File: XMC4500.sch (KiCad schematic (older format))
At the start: 1 part

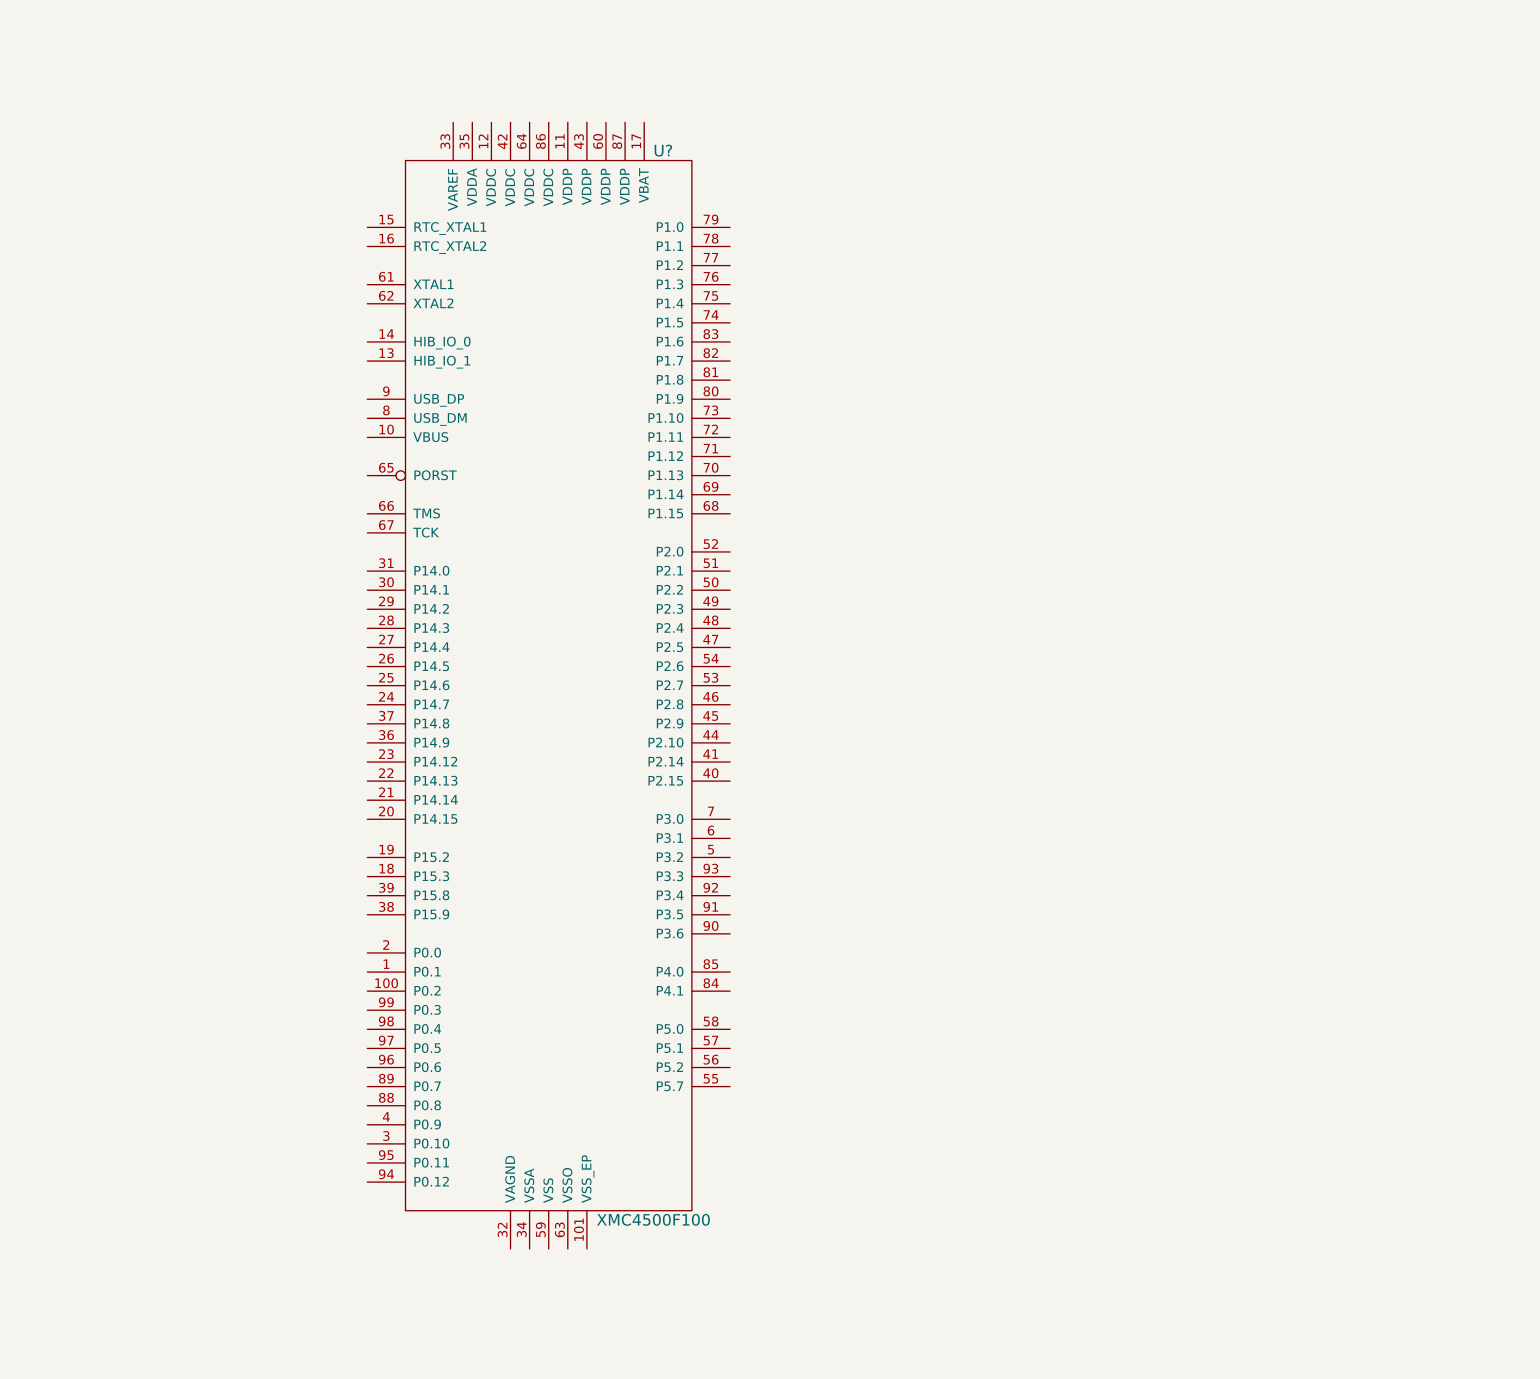
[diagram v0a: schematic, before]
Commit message: Added capacitors for XMC chip, diagram of power tree, and more connectors.
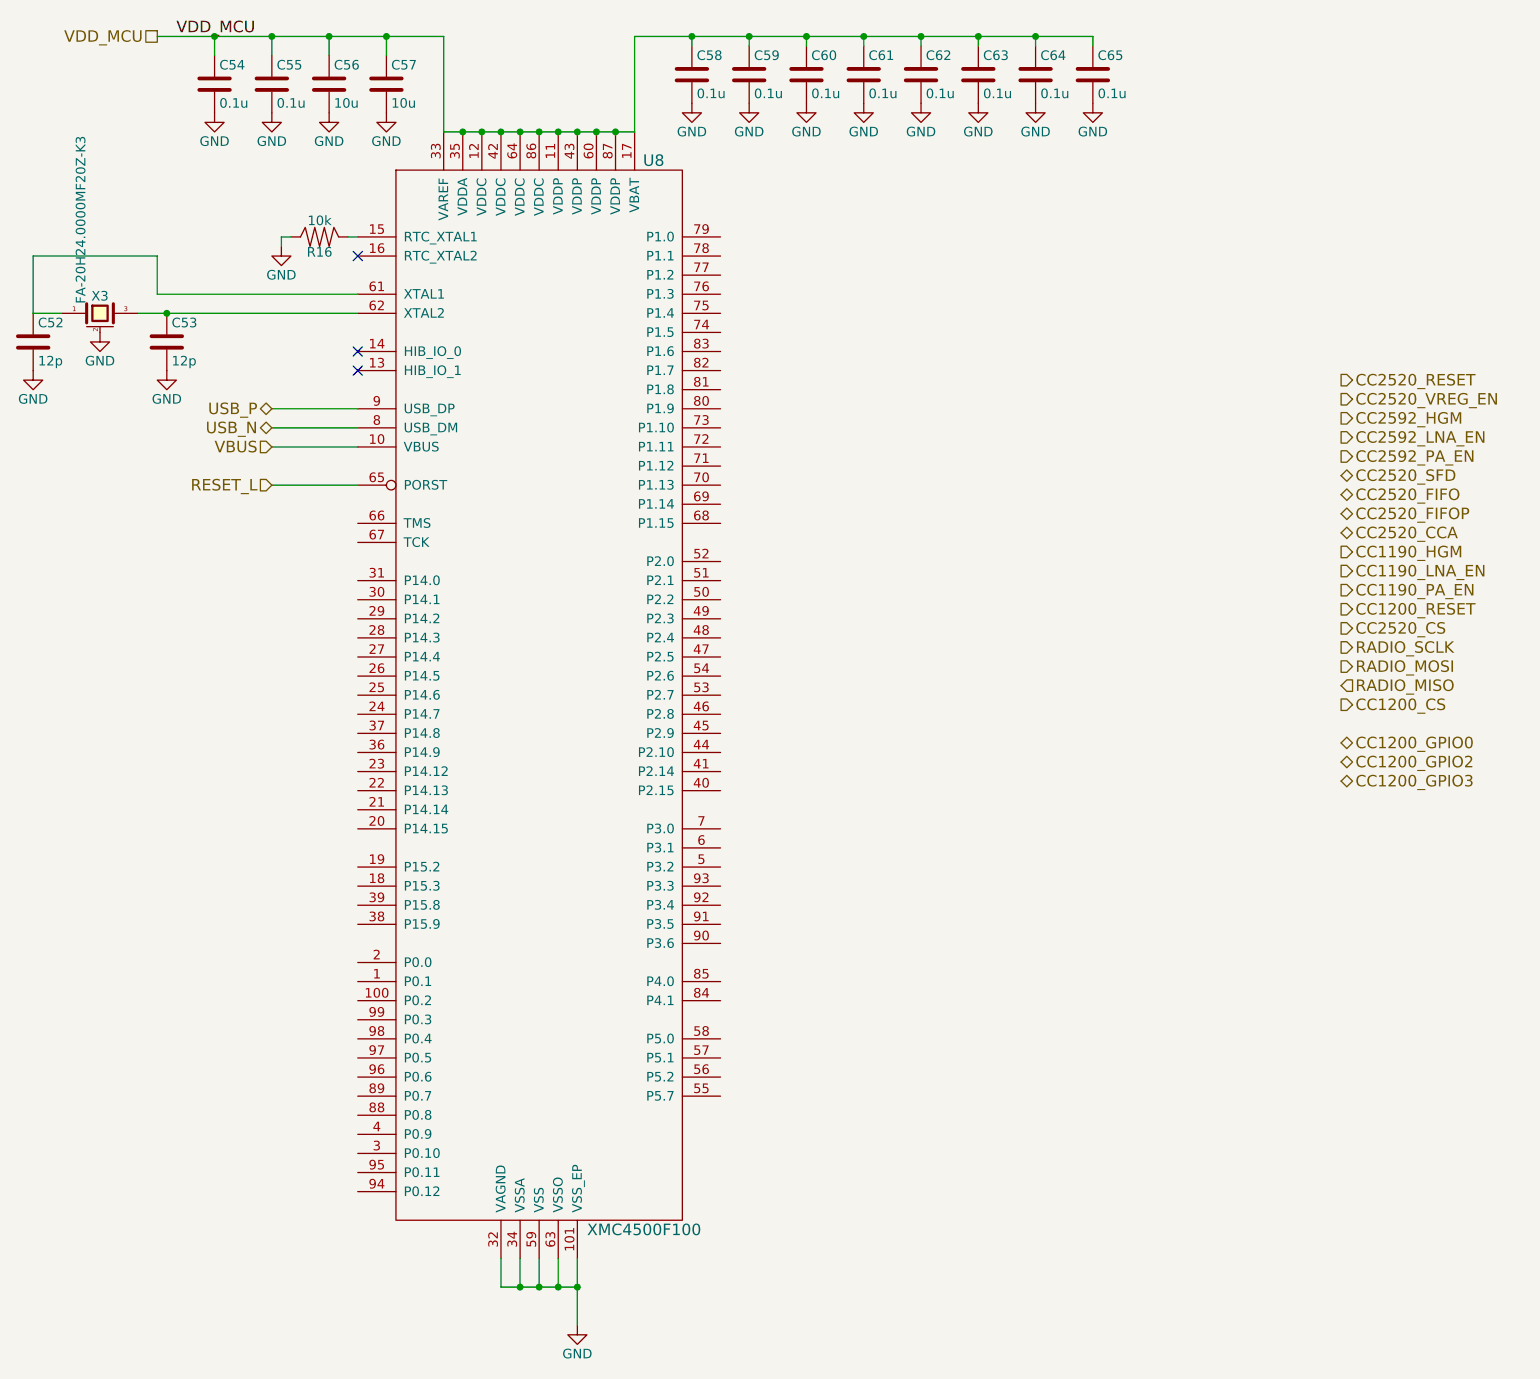
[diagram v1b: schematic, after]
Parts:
- removed U?: XMC4500F100, symbol XMC4500F100
- added C52, C53: 12p, Capacitors_SMD:C_0402, symbol C
- added C54, C55, C58, C59, C60, C61, C62, C63, C64, C65: 0.1u, Capacitors_SMD:C_0402, symbol C
- added C56, C57: 10u, Capacitors_SMD:C_0603, symbol C
- added R16: 10k, Resistors_SMD:R_0402, symbol R
- added U8: XMC4500F100, Housings_QFP:LQFP-100-1EP_14x14mm_Pitch0.5mm, symbol XMC4500F100
- added X3: FA-20H24.0000MF20Z-K3, Crystals_Oscillators_SMD:FA-20H, symbol CRYSTAL_SMD
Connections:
- new net: R16.1, U8.15 (RTC_XTAL1)
- new net: C52.1, U8.61 (XTAL1), X3.1
- new net: C53.1, U8.62 (XTAL2), X3.3
- new net GND: C52.2, C53.2, C54.2, C55.2, C56.2, C57.2, C58.2, C59.2, C60.2, C61.2, C62.2, C63.2, C64.2, C65.2, R16.2, U8.101 (VSS_EP), U8.32 (VAGND), U8.34 (VSSA), U8.59 (VSS), U8.63 (VSSO), X3.2 (gnd), X3.4 (gnd)
- new net RESET_L: U8.65 (PORST)
- new net USB_N: U8.8 (USB_DM)
- new net USB_P: U8.9 (USB_DP)
- new net VBUS: U8.10 (VBUS)
- new net VDD_MCU: C54.1, C55.1, C56.1, C57.1, C58.1, C59.1, C60.1, C61.1, C62.1, C63.1, C64.1, C65.1, U8.11 (VDDP), U8.12 (VDDC), U8.17 (VBAT), U8.33 (VAREF), U8.35 (VDDA), U8.42 (VDDC), U8.43 (VDDP), U8.60 (VDDP), U8.64 (VDDC), U8.86 (VDDC), U8.87 (VDDP)
- no-connect marks 0 -> 3

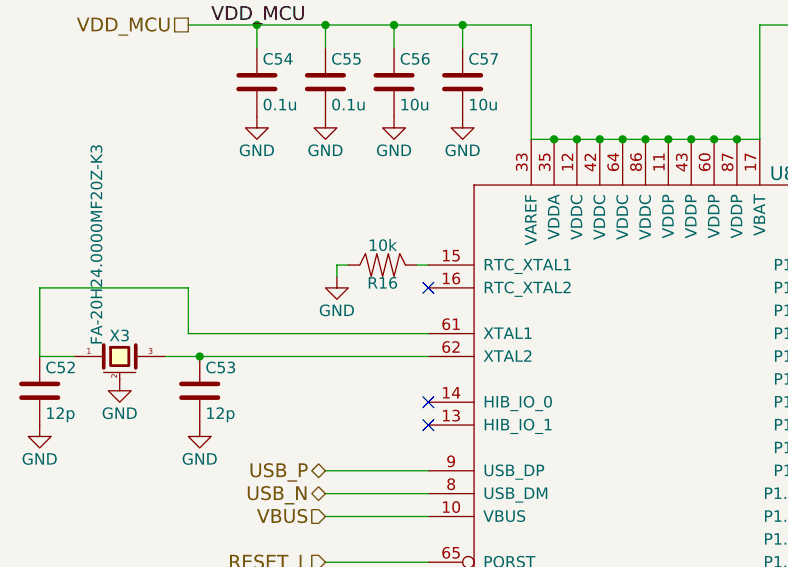
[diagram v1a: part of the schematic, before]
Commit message: Added 3.3V LDO
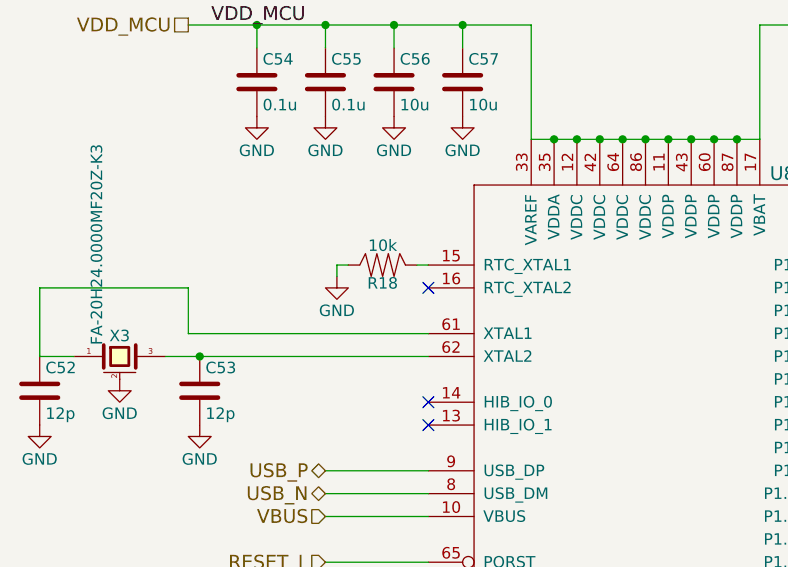
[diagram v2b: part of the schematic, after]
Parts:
- renumbered R16 to R18
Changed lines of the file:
@@
 $Descr A4 11693 8268
 encoding utf-8
-Sheet 4 4
+Sheet 4 7
 Title ""
 Date ""
@@
 $EndComp
 $Comp
-L GND #PWR80
+L GND #PWR080
 U 1 1 55BD550B
 P 4500 7450
-F 0 "#PWR80" H 4500 7200 50  0001 C CNN
+F 0 "#PWR080" H 4500 7200 50  0001 C CNN
 F 1 "GND" H 4500 7300 50  0000 C CNN
 F 2 "" H 4500 7450 60  0000 C CNN
@@
 $EndComp
 $Comp
-L GND #PWR81
+L GND #PWR081
 U 1 1 55BD5744
 P 5100 1050
-F 0 "#PWR81" H 5100 800 50  0001 C CNN
+F 0 "#PWR081" H 5100 800 50  0001 C CNN
 F 1 "GND" H 5100 900 50  0000 C CNN
 F 2 "" H 5100 1050 60  0000 C CNN
@@
 $EndComp
 $Comp
-L GND #PWR82
+L GND #PWR082
 U 1 1 55BD5822
 P 5400 1050
-F 0 "#PWR82" H 5400 800 50  0001 C CNN
+F 0 "#PWR082" H 5400 800 50  0001 C CNN
 F 1 "GND" H 5400 900 50  0000 C CNN
 F 2 "" H 5400 1050 60  0000 C CNN
@@
 $EndComp
 $Comp
-L GND #PWR83
+L GND #PWR083
 U 1 1 55BD589D
 P 5700 1050
-F 0 "#PWR83" H 5700 800 50  0001 C CNN
+F 0 "#PWR083" H 5700 800 50  0001 C CNN
 F 1 "GND" H 5700 900 50  0000 C CNN
 F 2 "" H 5700 1050 60  0000 C CNN
@@
 $EndComp
 $Comp
-L GND #PWR84
+L GND #PWR084
 U 1 1 55BD58A9
 P 6000 1050
-F 0 "#PWR84" H 6000 800 50  0001 C CNN
+F 0 "#PWR084" H 6000 800 50  0001 C CNN
 F 1 "GND" H 6000 900 50  0000 C CNN
 F 2 "" H 6000 1050 60  0000 C CNN
@@
 $EndComp
 $Comp
-L GND #PWR85
+L GND #PWR085
 U 1 1 55BD5AC7
 P 6300 1050
-F 0 "#PWR85" H 6300 800 50  0001 C CNN
+F 0 "#PWR085" H 6300 800 50  0001 C CNN
 F 1 "GND" H 6300 900 50  0000 C CNN
 F 2 "" H 6300 1050 60  0000 C CNN
@@
 $EndComp
 $Comp
-L GND #PWR86
+L GND #PWR086
 U 1 1 55BD5AD3
 P 6600 1050
-F 0 "#PWR86" H 6600 800 50  0001 C CNN
+F 0 "#PWR086" H 6600 800 50  0001 C CNN
 F 1 "GND" H 6600 900 50  0000 C CNN
 F 2 "" H 6600 1050 60  0000 C CNN
@@
 $EndComp
 $Comp
-L GND #PWR87
+L GND #PWR087
 U 1 1 55BD5ADF
 P 6900 1050
-F 0 "#PWR87" H 6900 800 50  0001 C CNN
+F 0 "#PWR087" H 6900 800 50  0001 C CNN
 F 1 "GND" H 6900 900 50  0000 C CNN
 F 2 "" H 6900 1050 60  0000 C CNN
@@
 $EndComp
 $Comp
-L GND #PWR88
+L GND #PWR088
 U 1 1 55BD5AEB
 P 7200 1050
-F 0 "#PWR88" H 7200 800 50  0001 C CNN
+F 0 "#PWR088" H 7200 800 50  0001 C CNN
 F 1 "GND" H 7200 900 50  0000 C CNN
 F 2 "" H 7200 1050 60  0000 C CNN
@@
 $EndComp
 $Comp
-L GND #PWR78
+L GND #PWR089
 U 1 1 55BD5E40
 P 3200 1100
-F 0 "#PWR78" H 3200 850 50  0001 C CNN
+F 0 "#PWR089" H 3200 850 50  0001 C CNN
 F 1 "GND" H 3200 950 50  0000 C CNN
 F 2 "" H 3200 1100 60  0000 C CNN
@@
 $EndComp
 $Comp
-L GND #PWR79
+L GND #PWR090
 U 1 1 55BD5E6C
 P 3500 1100
-F 0 "#PWR79" H 3500 850 50  0001 C CNN
+F 0 "#PWR090" H 3500 850 50  0001 C CNN
 F 1 "GND" H 3500 950 50  0000 C CNN
 F 2 "" H 3500 1100 60  0000 C CNN
@@
 $EndComp
 $Comp
-L GND #PWR76
+L GND #PWR091
 U 1 1 55BD6192
 P 2900 1100
-F 0 "#PWR76" H 2900 850 50  0001 C CNN
+F 0 "#PWR091" H 2900 850 50  0001 C CNN
 F 1 "GND" H 2900 950 50  0000 C CNN
 F 2 "" H 2900 1100 60  0000 C CNN
@@
 $EndComp
 $Comp
-L GND #PWR75
+L GND #PWR092
 U 1 1 55BD61C4
 P 2600 1100
-F 0 "#PWR75" H 2600 850 50  0001 C CNN
+F 0 "#PWR092" H 2600 850 50  0001 C CNN
 F 1 "GND" H 2600 950 50  0000 C CNN
 F 2 "" H 2600 1100 60  0000 C CNN
@@
 NoConn ~ 3350 1850
 $Comp
-L GND #PWR77
+L GND #PWR093
 U 1 1 55BD7C61
 P 2950 1800
-F 0 "#PWR77" H 2950 1550 50  0001 C CNN
+F 0 "#PWR093" H 2950 1550 50  0001 C CNN
 F 1 "GND" H 2950 1650 50  0000 C CNN
 F 2 "" H 2950 1800 60  0000 C CNN
@@
 	2950 1800 2950 1750
 $Comp
-L R R16
+L R R18
 U 1 1 55BD7CEC
 P 3150 1750
-F 0 "R16" V 3230 1750 50  0000 C CNN
+F 0 "R18" V 3230 1750 50  0000 C CNN
 F 1 "10k" V 3065 1750 50  0000 C CNN
 F 2 "Resistors_SMD:R_0402" V 3080 1750 30  0001 C CNN
@@
 $EndComp
 $Comp
-L GND #PWR73
+L GND #PWR094
 U 1 1 55BD886E
 P 2000 2250
-F 0 "#PWR73" H 2000 2000 50  0001 C CNN
+F 0 "#PWR094" H 2000 2000 50  0001 C CNN
 F 1 "GND" H 2000 2100 50  0000 C CNN
 F 2 "" H 2000 2250 60  0000 C CNN
@@
 $EndComp
 $Comp
-L GND #PWR74
+L GND #PWR095
 U 1 1 55BD9CC6
 P 2350 2450
-F 0 "#PWR74" H 2350 2200 50  0001 C CNN
+F 0 "#PWR095" H 2350 2200 50  0001 C CNN
 F 1 "GND" H 2350 2300 50  0000 C CNN
 F 2 "" H 2350 2450 60  0000 C CNN
@@
 $EndComp
 $Comp
-L GND #PWR72
+L GND #PWR096
 U 1 1 55BD9D04
 P 1650 2450
-F 0 "#PWR72" H 1650 2200 50  0001 C CNN
+F 0 "#PWR096" H 1650 2200 50  0001 C CNN
 F 1 "GND" H 1650 2300 50  0000 C CNN
 F 2 "" H 1650 2450 60  0000 C CNN
